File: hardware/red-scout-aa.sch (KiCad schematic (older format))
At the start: 31 parts, among them P1 SNAP, P2 SNAP, P3 SNAP, P4 SNAP, P5 SNAP, P6 SNAP, P7 SNAP, P8 SNAP, U1 SM200

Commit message: Placed all parts on PCB.
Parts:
- BT1: footprint (none) -> _CrumpPrints:AA_battery_holder_12BH321P-GR
- D1, D2: footprint (none) -> LEDs:LED-0805
- P1, P2, P3, P4, P5, P6, P7, P8: footprint (none) -> _CrumpPrints:16_snap
- R1, R10, R11, R12, R13, R14, R15, R16, R17, R18, R19, R2, R3, R4, R5, R6, R7, R8, R9: footprint (none) -> Resistors_SMD:R_0805_HandSoldering
- U1: footprint (none) -> _CrumpPrints:SM200
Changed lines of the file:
@@
 F 0 "U1" H 3550 4800 60  0000 C CNN
 F 1 "SM200" H 3550 950 60  0000 C CNN
-F 2 "" H 4250 4350 60  0000 C CNN
+F 2 "_CrumpPrints:SM200" H 4250 4350 60  0001 C CNN
 F 3 "" H 4250 4350 60  0000 C CNN
 	1    3550 3100
@@
 F 0 "BT1" H 5600 2200 50  0000 C CNN
 F 1 "BATTERY" H 5600 1810 50  0000 C CNN
-F 2 "" H 5600 2000 60  0000 C CNN
+F 2 "_CrumpPrints:AA_battery_holder_12BH321P-GR" H 5600 2000 60  0001 C CNN
 F 3 "" H 5600 2000 60  0000 C CNN
 	1    5600 2000
@@
 F 0 "R7" V 7630 2150 40  0000 C CNN
 F 1 "PD" V 7557 2151 40  0000 C CNN
-F 2 "" V 7480 2150 30  0000 C CNN
+F 2 "Resistors_SMD:R_0805_HandSoldering" V 7480 2150 30  0001 C CNN
 F 3 "" H 7550 2150 30  0000 C CNN
 	1    7550 2150
@@
 F 0 "P2" H 7550 1700 50  0000 C CNN
 F 1 "SNAP" V 7650 1600 50  0000 C CNN
-F 2 "" H 7550 1600 60  0000 C CNN
+F 2 "_CrumpPrints:16_snap" H 7550 1600 60  0001 C CNN
 F 3 "" H 7550 1600 60  0000 C CNN
 	1    7550 1600
@@
 F 0 "R2" V 5580 3850 40  0000 C CNN
 F 1 "1K" V 5507 3851 40  0000 C CNN
-F 2 "" V 5430 3850 30  0000 C CNN
+F 2 "Resistors_SMD:R_0805_HandSoldering" V 5430 3850 30  0001 C CNN
 F 3 "" H 5500 3850 30  0000 C CNN
 	1    5500 3850
@@
 F 0 "R3" V 5880 3850 40  0000 C CNN
 F 1 "1K" V 5807 3851 40  0000 C CNN
-F 2 "" V 5730 3850 30  0000 C CNN
+F 2 "Resistors_SMD:R_0805_HandSoldering" V 5730 3850 30  0001 C CNN
 F 3 "" H 5800 3850 30  0000 C CNN
 	1    5800 3850
@@
 F 0 "D1" H 5500 4500 50  0000 C CNN
 F 1 "LED" H 5500 4300 50  0000 C CNN
-F 2 "" H 5500 4400 60  0000 C CNN
+F 2 "LEDs:LED-0805" H 5500 4400 60  0001 C CNN
 F 3 "" H 5500 4400 60  0000 C CNN
 	1    5500 4400
@@
 F 0 "D2" H 5800 4500 50  0000 C CNN
 F 1 "LED" H 5800 4300 50  0000 C CNN
-F 2 "" H 5800 4400 60  0000 C CNN
+F 2 "LEDs:LED-0805" H 5800 4400 60  0001 C CNN
 F 3 "" H 5800 4400 60  0000 C CNN
 	1    5800 4400
@@
 F 0 "R6" V 7480 2150 40  0000 C CNN
 F 1 "PU" V 7407 2151 40  0000 C CNN
-F 2 "" V 7330 2150 30  0000 C CNN
+F 2 "Resistors_SMD:R_0805_HandSoldering" V 7330 2150 30  0001 C CNN
 F 3 "" H 7400 2150 30  0000 C CNN
 	1    7400 2150
@@
 F 0 "R5" V 7130 2150 40  0000 C CNN
 F 1 "PD" V 7057 2151 40  0000 C CNN
-F 2 "" V 6980 2150 30  0000 C CNN
+F 2 "Resistors_SMD:R_0805_HandSoldering" V 6980 2150 30  0001 C CNN
 F 3 "" H 7050 2150 30  0000 C CNN
 	1    7050 2150
@@
 F 0 "P1" H 7050 1700 50  0000 C CNN
 F 1 "SNAP" V 7150 1600 50  0000 C CNN
-F 2 "" H 7050 1600 60  0000 C CNN
+F 2 "_CrumpPrints:16_snap" H 7050 1600 60  0001 C CNN
 F 3 "" H 7050 1600 60  0000 C CNN
 	1    7050 1600
@@
 F 0 "R4" V 6980 2150 40  0000 C CNN
 F 1 "PU" V 6907 2151 40  0000 C CNN
-F 2 "" V 6830 2150 30  0000 C CNN
+F 2 "Resistors_SMD:R_0805_HandSoldering" V 6830 2150 30  0001 C CNN
 F 3 "" H 6900 2150 30  0000 C CNN
 	1    6900 2150
@@
 F 0 "R11" V 8630 2150 40  0000 C CNN
 F 1 "PD" V 8557 2151 40  0000 C CNN
-F 2 "" V 8480 2150 30  0000 C CNN
+F 2 "Resistors_SMD:R_0805_HandSoldering" V 8480 2150 30  0001 C CNN
 F 3 "" H 8550 2150 30  0000 C CNN
 	1    8550 2150
@@
 F 0 "P4" H 8550 1700 50  0000 C CNN
 F 1 "SNAP" V 8650 1600 50  0000 C CNN
-F 2 "" H 8550 1600 60  0000 C CNN
+F 2 "_CrumpPrints:16_snap" H 8550 1600 60  0001 C CNN
 F 3 "" H 8550 1600 60  0000 C CNN
 	1    8550 1600
@@
 F 0 "R10" V 8480 2150 40  0000 C CNN
 F 1 "PU" V 8407 2151 40  0000 C CNN
-F 2 "" V 8330 2150 30  0000 C CNN
+F 2 "Resistors_SMD:R_0805_HandSoldering" V 8330 2150 30  0001 C CNN
 F 3 "" H 8400 2150 30  0000 C CNN
 	1    8400 2150
@@
 F 0 "R9" V 8130 2150 40  0000 C CNN
 F 1 "PD" V 8057 2151 40  0000 C CNN
-F 2 "" V 7980 2150 30  0000 C CNN
+F 2 "Resistors_SMD:R_0805_HandSoldering" V 7980 2150 30  0001 C CNN
 F 3 "" H 8050 2150 30  0000 C CNN
 	1    8050 2150
@@
 F 0 "P3" H 8050 1700 50  0000 C CNN
 F 1 "SNAP" V 8150 1600 50  0000 C CNN
-F 2 "" H 8050 1600 60  0000 C CNN
+F 2 "_CrumpPrints:16_snap" H 8050 1600 60  0001 C CNN
 F 3 "" H 8050 1600 60  0000 C CNN
 	1    8050 1600
@@
 F 0 "R8" V 7980 2150 40  0000 C CNN
 F 1 "PU" V 7907 2151 40  0000 C CNN
-F 2 "" V 7830 2150 30  0000 C CNN
+F 2 "Resistors_SMD:R_0805_HandSoldering" V 7830 2150 30  0001 C CNN
 F 3 "" H 7900 2150 30  0000 C CNN
 	1    7900 2150
@@
 F 0 "R15" V 9630 2150 40  0000 C CNN
 F 1 "PD" V 9557 2151 40  0000 C CNN
-F 2 "" V 9480 2150 30  0000 C CNN
+F 2 "Resistors_SMD:R_0805_HandSoldering" V 9480 2150 30  0001 C CNN
 F 3 "" H 9550 2150 30  0000 C CNN
 	1    9550 2150
@@
 F 0 "P6" H 9550 1700 50  0000 C CNN
 F 1 "SNAP" V 9650 1600 50  0000 C CNN
-F 2 "" H 9550 1600 60  0000 C CNN
+F 2 "_CrumpPrints:16_snap" H 9550 1600 60  0001 C CNN
 F 3 "" H 9550 1600 60  0000 C CNN
 	1    9550 1600
@@
 F 0 "R14" V 9480 2150 40  0000 C CNN
 F 1 "PU" V 9407 2151 40  0000 C CNN
-F 2 "" V 9330 2150 30  0000 C CNN
+F 2 "Resistors_SMD:R_0805_HandSoldering" V 9330 2150 30  0001 C CNN
 F 3 "" H 9400 2150 30  0000 C CNN
 	1    9400 2150
@@
 F 0 "R13" V 9130 2150 40  0000 C CNN
 F 1 "PD" V 9057 2151 40  0000 C CNN
-F 2 "" V 8980 2150 30  0000 C CNN
+F 2 "Resistors_SMD:R_0805_HandSoldering" V 8980 2150 30  0001 C CNN
 F 3 "" H 9050 2150 30  0000 C CNN
 	1    9050 2150
@@
 F 0 "P5" H 9050 1700 50  0000 C CNN
 F 1 "SNAP" V 9150 1600 50  0000 C CNN
-F 2 "" H 9050 1600 60  0000 C CNN
+F 2 "_CrumpPrints:16_snap" H 9050 1600 60  0001 C CNN
 F 3 "" H 9050 1600 60  0000 C CNN
 	1    9050 1600
@@
 F 0 "R12" V 8980 2150 40  0000 C CNN
 F 1 "PU" V 8907 2151 40  0000 C CNN
-F 2 "" V 8830 2150 30  0000 C CNN
+F 2 "Resistors_SMD:R_0805_HandSoldering" V 8830 2150 30  0001 C CNN
 F 3 "" H 8900 2150 30  0000 C CNN
 	1    8900 2150
@@
 F 0 "R19" V 10630 2150 40  0000 C CNN
 F 1 "PD" V 10557 2151 40  0000 C CNN
-F 2 "" V 10480 2150 30  0000 C CNN
+F 2 "Resistors_SMD:R_0805_HandSoldering" V 10480 2150 30  0001 C CNN
 F 3 "" H 10550 2150 30  0000 C CNN
 	1    10550 2150
@@
 F 0 "P8" H 10550 1700 50  0000 C CNN
 F 1 "SNAP" V 10650 1600 50  0000 C CNN
-F 2 "" H 10550 1600 60  0000 C CNN
+F 2 "_CrumpPrints:16_snap" H 10550 1600 60  0001 C CNN
 F 3 "" H 10550 1600 60  0000 C CNN
 	1    10550 1600
@@
 F 0 "R18" V 10480 2150 40  0000 C CNN
 F 1 "PU" V 10407 2151 40  0000 C CNN
-F 2 "" V 10330 2150 30  0000 C CNN
+F 2 "Resistors_SMD:R_0805_HandSoldering" V 10330 2150 30  0001 C CNN
 F 3 "" H 10400 2150 30  0000 C CNN
 	1    10400 2150
@@
 F 0 "R17" V 10130 2150 40  0000 C CNN
 F 1 "PD" V 10057 2151 40  0000 C CNN
-F 2 "" V 9980 2150 30  0000 C CNN
+F 2 "Resistors_SMD:R_0805_HandSoldering" V 9980 2150 30  0001 C CNN
 F 3 "" H 10050 2150 30  0000 C CNN
 	1    10050 2150
@@
 F 0 "P7" H 10050 1700 50  0000 C CNN
 F 1 "SNAP" V 10150 1600 50  0000 C CNN
-F 2 "" H 10050 1600 60  0000 C CNN
+F 2 "_CrumpPrints:16_snap" H 10050 1600 60  0001 C CNN
 F 3 "" H 10050 1600 60  0000 C CNN
 	1    10050 1600
@@
 F 0 "R16" V 9980 2150 40  0000 C CNN
 F 1 "PU" V 9907 2151 40  0000 C CNN
-F 2 "" V 9830 2150 30  0000 C CNN
+F 2 "Resistors_SMD:R_0805_HandSoldering" V 9830 2150 30  0001 C CNN
 F 3 "" H 9900 2150 30  0000 C CNN
 	1    9900 2150
@@
 F 0 "R1" V 2580 3250 40  0000 C CNN
 F 1 "10K" V 2507 3251 40  0000 C CNN
-F 2 "" V 2430 3250 30  0000 C CNN
+F 2 "Resistors_SMD:R_0805_HandSoldering" V 2430 3250 30  0001 C CNN
 F 3 "" H 2500 3250 30  0000 C CNN
 	1    2500 3250

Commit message: Finished placing and routing board.
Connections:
- net PWM6: no longer U1.D3 (GPIO_7)
- net PWM7: now also U1.D3 (GPIO_7)
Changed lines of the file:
@@
 LIBS:valves
 LIBS:crumpschemes
+LIBS:red-scout-aa-cache
 EELAYER 25 0
 EELAYER END
@@
 	10200 1850 10200 1900
 Text GLabel 4400 2250 2    60   Input ~ 0
-PWM6
+PWM7
 Wire Wire Line
 	4400 2250 4300 2250

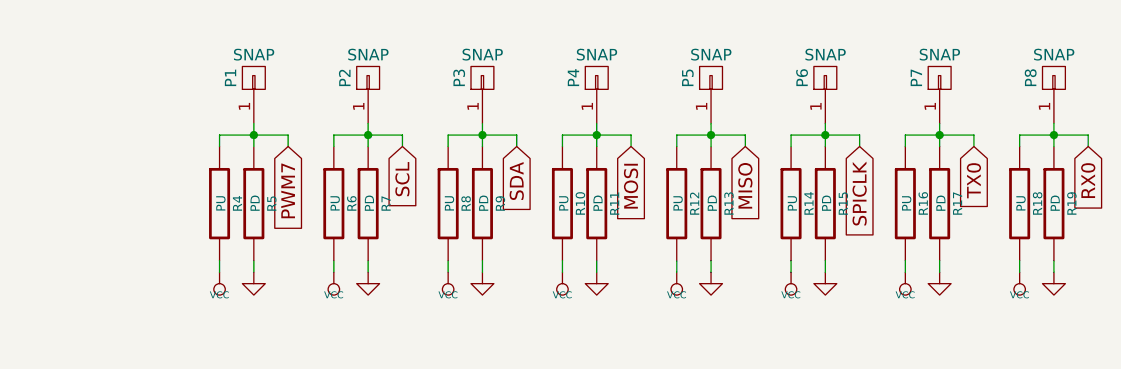
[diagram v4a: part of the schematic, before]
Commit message: Add IO pin headers to schematic.
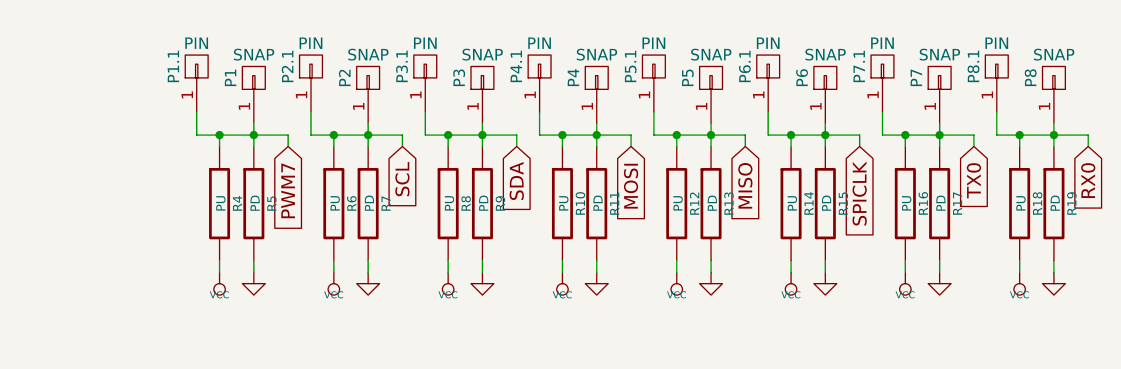
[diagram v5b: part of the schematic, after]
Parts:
- added P1.1, P2.1, P3.1, P4.1, P5.1, P6.1, P7.1, P8.1: PIN, _CrumpPrints:16_snap, symbol CONN_01X01
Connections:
- net MISO: now also P5.1.1 (P1)
- net MOSI: now also P4.1.1 (P1)
- net PWM7: now also P1.1.1 (P1)
- net RX0: now also P8.1.1 (P1)
- net SCL: now also P2.1.1 (P1)
- net SDA: now also P3.1.1 (P1)
- net SPICLK: now also P6.1.1 (P1)
- net TX0: now also P7.1.1 (P1)

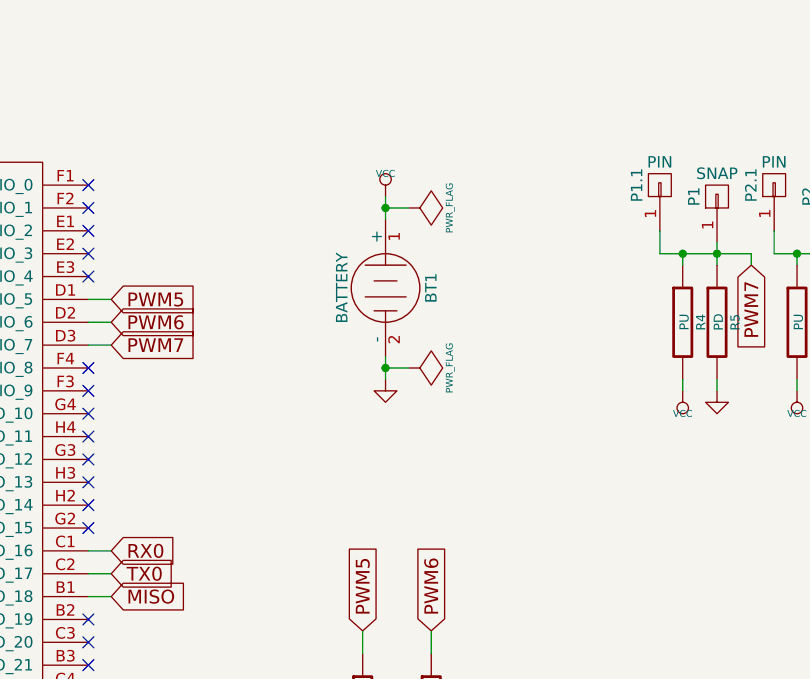
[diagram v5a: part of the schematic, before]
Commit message: Add power switch to schematic.
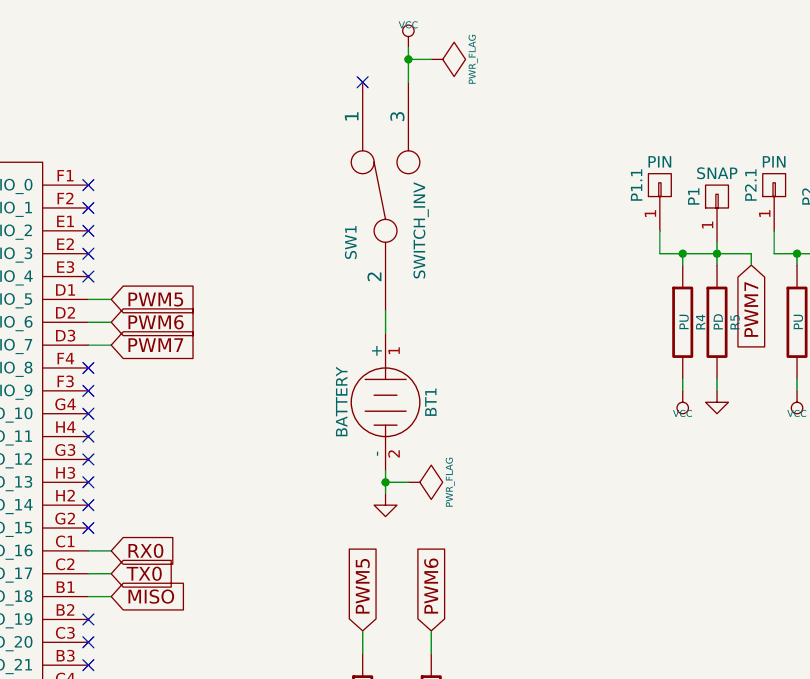
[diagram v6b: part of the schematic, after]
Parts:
- added SW1: SWITCH_INV, symbol SWITCH_INV
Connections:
- net VCC: now also SW1.3; no longer BT1.1 (+)
- new net: BT1.1 (+), SW1.2
- no-connect marks 24 -> 25
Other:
- moved on the sheet: BT1
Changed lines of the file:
@@
 L BATTERY BT1
 U 1 1 54F7F32F
-P 5600 2000
-F 0 "BT1" H 5600 2200 50  0000 C CNN
-F 1 "BATTERY" H 5600 1810 50  0000 C CNN
-F 2 "_CrumpPrints:AA_battery_holder_12BH321P-GR" H 5600 2000 60  0001 C CNN
-F 3 "" H 5600 2000 60  0000 C CNN
-	1    5600 2000
+P 5600 2500
+F 0 "BT1" H 5600 2700 50  0000 C CNN
+F 1 "BATTERY" H 5600 2310 50  0000 C CNN
+F 2 "_CrumpPrints:AA_battery_holder_12BH321P-GR" H 5600 2500 60  0001 C CNN
+F 3 "" H 5600 2500 60  0000 C CNN
+	1    5600 2500
 	0    1    1    0
 $EndComp
@@
 L GND #PWR02
 U 1 1 54F7F3EE
-P 5600 2400
-F 0 "#PWR02" H 5600 2400 30  0001 C CNN
-F 1 "GND" H 5600 2330 30  0001 C CNN
-F 2 "" H 5600 2400 60  0000 C CNN
-F 3 "" H 5600 2400 60  0000 C CNN
-	1    5600 2400
+P 5600 2900
+F 0 "#PWR02" H 5600 2900 30  0001 C CNN
+F 1 "GND" H 5600 2830 30  0001 C CNN
+F 2 "" H 5600 2900 60  0000 C CNN
+F 3 "" H 5600 2900 60  0000 C CNN
+	1    5600 2900
 	1    0    0    -1
 $EndComp
@@
 L VCC #PWR03
 U 1 1 54F7F402
-P 5600 1600
-F 0 "#PWR03" H 5600 1700 30  0001 C CNN
-F 1 "VCC" H 5600 1700 30  0000 C CNN
-F 2 "" H 5600 1600 60  0000 C CNN
-F 3 "" H 5600 1600 60  0000 C CNN
-	1    5600 1600
+P 5700 950
+F 0 "#PWR03" H 5700 1050 30  0001 C CNN
+F 1 "VCC" H 5700 1050 30  0000 C CNN
+F 2 "" H 5700 950 60  0000 C CNN
+F 3 "" H 5700 950 60  0000 C CNN
+	1    5700 950
 	1    0    0    -1
 $EndComp
@@
 L PWR_FLAG #FLG05
 U 1 1 54F7F51D
-P 5700 1650
-F 0 "#FLG05" H 5700 1745 30  0001 C CNN
-F 1 "PWR_FLAG" H 5700 1830 30  0000 C CNN
-F 2 "" H 5700 1650 60  0000 C CNN
-F 3 "" H 5700 1650 60  0000 C CNN
-	1    5700 1650
+P 5800 1000
+F 0 "#FLG05" H 5800 1095 30  0001 C CNN
+F 1 "PWR_FLAG" H 5800 1180 30  0000 C CNN
+F 2 "" H 5800 1000 60  0000 C CNN
+F 3 "" H 5800 1000 60  0000 C CNN
+	1    5800 1000
 	0    1    1    0
 $EndComp
@@
 L PWR_FLAG #FLG06
 U 1 1 54F7F531
-P 5700 2350
-F 0 "#FLG06" H 5700 2445 30  0001 C CNN
-F 1 "PWR_FLAG" H 5700 2530 30  0000 C CNN
-F 2 "" H 5700 2350 60  0000 C CNN
-F 3 "" H 5700 2350 60  0000 C CNN
-	1    5700 2350
+P 5700 2850
+F 0 "#FLG06" H 5700 2945 30  0001 C CNN
+F 1 "PWR_FLAG" H 5700 3030 30  0000 C CNN
+F 2 "" H 5700 2850 60  0000 C CNN
+F 3 "" H 5700 2850 60  0000 C CNN
+	1    5700 2850
 	0    1    1    0
 $EndComp
@@
 Connection ~ 2750 2350
 Wire Wire Line
-	5600 1600 5600 1700
-Wire Wire Line
-	5600 2300 5600 2400
+	5700 950  5700 1100
+Wire Wire Line
+	5600 2800 5600 2900
 Wire Wire Line
 	2650 2500 2650 2650
@@
 Connection ~ 2650 2550
 Wire Wire Line
-	5700 2350 5600 2350
-Connection ~ 5600 2350
-Wire Wire Line
-	5700 1650 5600 1650
-Connection ~ 5600 1650
+	5700 2850 5600 2850
+Connection ~ 5600 2850
+Wire Wire Line
+	5800 1000 5700 1000
+Connection ~ 5700 1000
 Wire Wire Line
 	7300 1850 7700 1850
@@
 	10300 1750 10300 1850
 Connection ~ 10400 1850
+$Comp
+L SWITCH_INV SW1
+U 1 1 558F5870
+P 5600 1600
+F 0 "SW1" H 5400 1750 50  0000 C CNN
+F 1 "SWITCH_INV" H 5450 1450 50  0000 C CNN
+F 2 "" H 5600 1600 60  0000 C CNN
+F 3 "" H 5600 1600 60  0000 C CNN
+	1    5600 1600
+	0    -1   -1   0
+$EndComp
+NoConn ~ 5500 1100
+Wire Wire Line
+	5600 2100 5600 2200
 $EndSCHEMATC

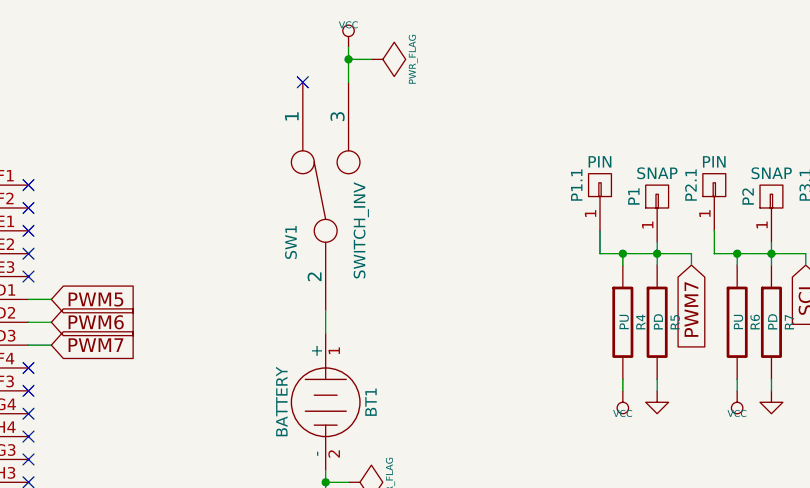
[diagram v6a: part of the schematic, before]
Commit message: Add power switch bypass to schematic.
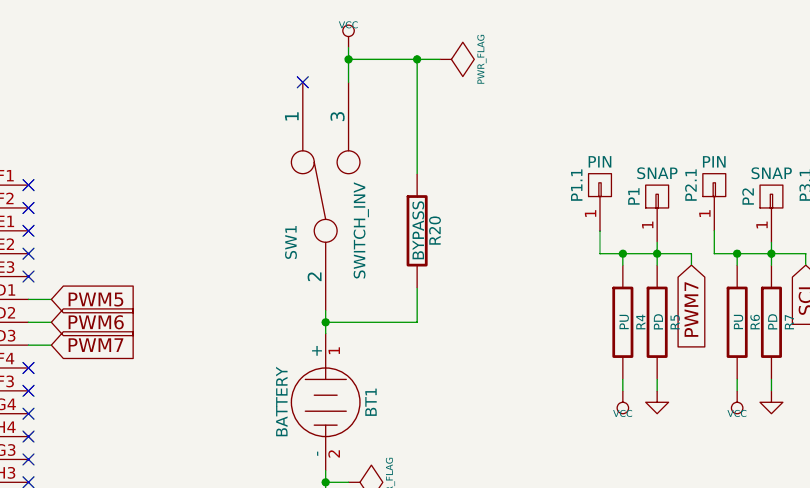
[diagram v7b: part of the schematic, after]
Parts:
- added R20: BYPASS, symbol R
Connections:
- net VCC: now also R20.1
- net at BT1.1 (+), SW1.2: now also R20.2
